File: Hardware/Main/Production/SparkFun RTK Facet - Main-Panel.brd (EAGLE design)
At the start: 138.6 x 187.7 mm, 990 parts, among them J1 QWIIC_RIGHT_ANGLE, J16 QWIIC_RIGHT_ANGLE, J2 U.FL, J21 CORTEX_JTAG_DEBUG_PTH, J24 U.FL, J28 QWIIC_RIGHT_ANGLE, J32 CORTEX_JTAG_DEBUG_PTH, J35 U.FL, J39 QWIIC_RIGHT_ANGLE, J43 CORTEX_JTAG_DEBUG_PTH, J46 U.FL, J50 QWIIC_RIGHT_ANGLE, J54 CORTEX_JTAG_DEBUG_PTH, J57 U.FL, J6 U.FL, J61 QWIIC_RIGHT_ANGLE, J65 CORTEX_JTAG_DEBUG_PTH, J68 U.FL, J72 QWIIC_RIGHT_ANGLE, J76 CORTEX_JTAG_DEBUG_PTH, J79 U.FL, J83 QWIIC_RIGHT_ANGLE, J87 CORTEX_JTAG_DEBUG_PTH, J9 CORTEX_JTAG_DEBUG_PTH, Q1 MBT3904DW1T1, Q10 SIL2308, Q11 MBT3904DW1T1, Q12 SIL2308, Q13 MBT3904DW1T1, Q14 SIL2308, Q15 MBT3904DW1T1, Q16 SIL2308, Q2 MBT3904DW1T1, Q3 SIL2308, Q4 SIL2308, Q5 MBT3904DW1T1, Q6 SIL2308, Q7 MBT3904DW1T1, Q8 SIL2308, Q9 MBT3904DW1T1, U1 74HC4052D, U10 MCP73833, U11 U-BLOX_ZED-F9P, U12 AP2112K-3.3, U13 CH340C, U14 MAX17048, U15 MCP73833, U16 74HC4052D, U17 STLQ015, U18 AP2112K-3.3, U19 USB251XB, U2 3.3V, U20 ESP-WROOM-3232D, U21 3.3V, U22 U-BLOX_ZED-F9P, U23 CH340C, U24 MAX17048, U25 MCP73833, U26 74HC4052D, U27 STLQ015, U28 AP2112K-3.3, U29 USB251XB, U3 U-BLOX_ZED-F9P, U30 ESP-WROOM-3232D, U31 3.3V, U32 U-BLOX_ZED-F9P, U33 CH340C, U34 MAX17048, U35 MCP73833, U36 74HC4052D, U37 STLQ015, U38 AP2112K-3.3, U39 USB251XB, U4 STLQ015, U40 ESP-WROOM-3232D, U41 3.3V, U42 U-BLOX_ZED-F9P, U43 CH340C, U44 MAX17048, U45 MCP73833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

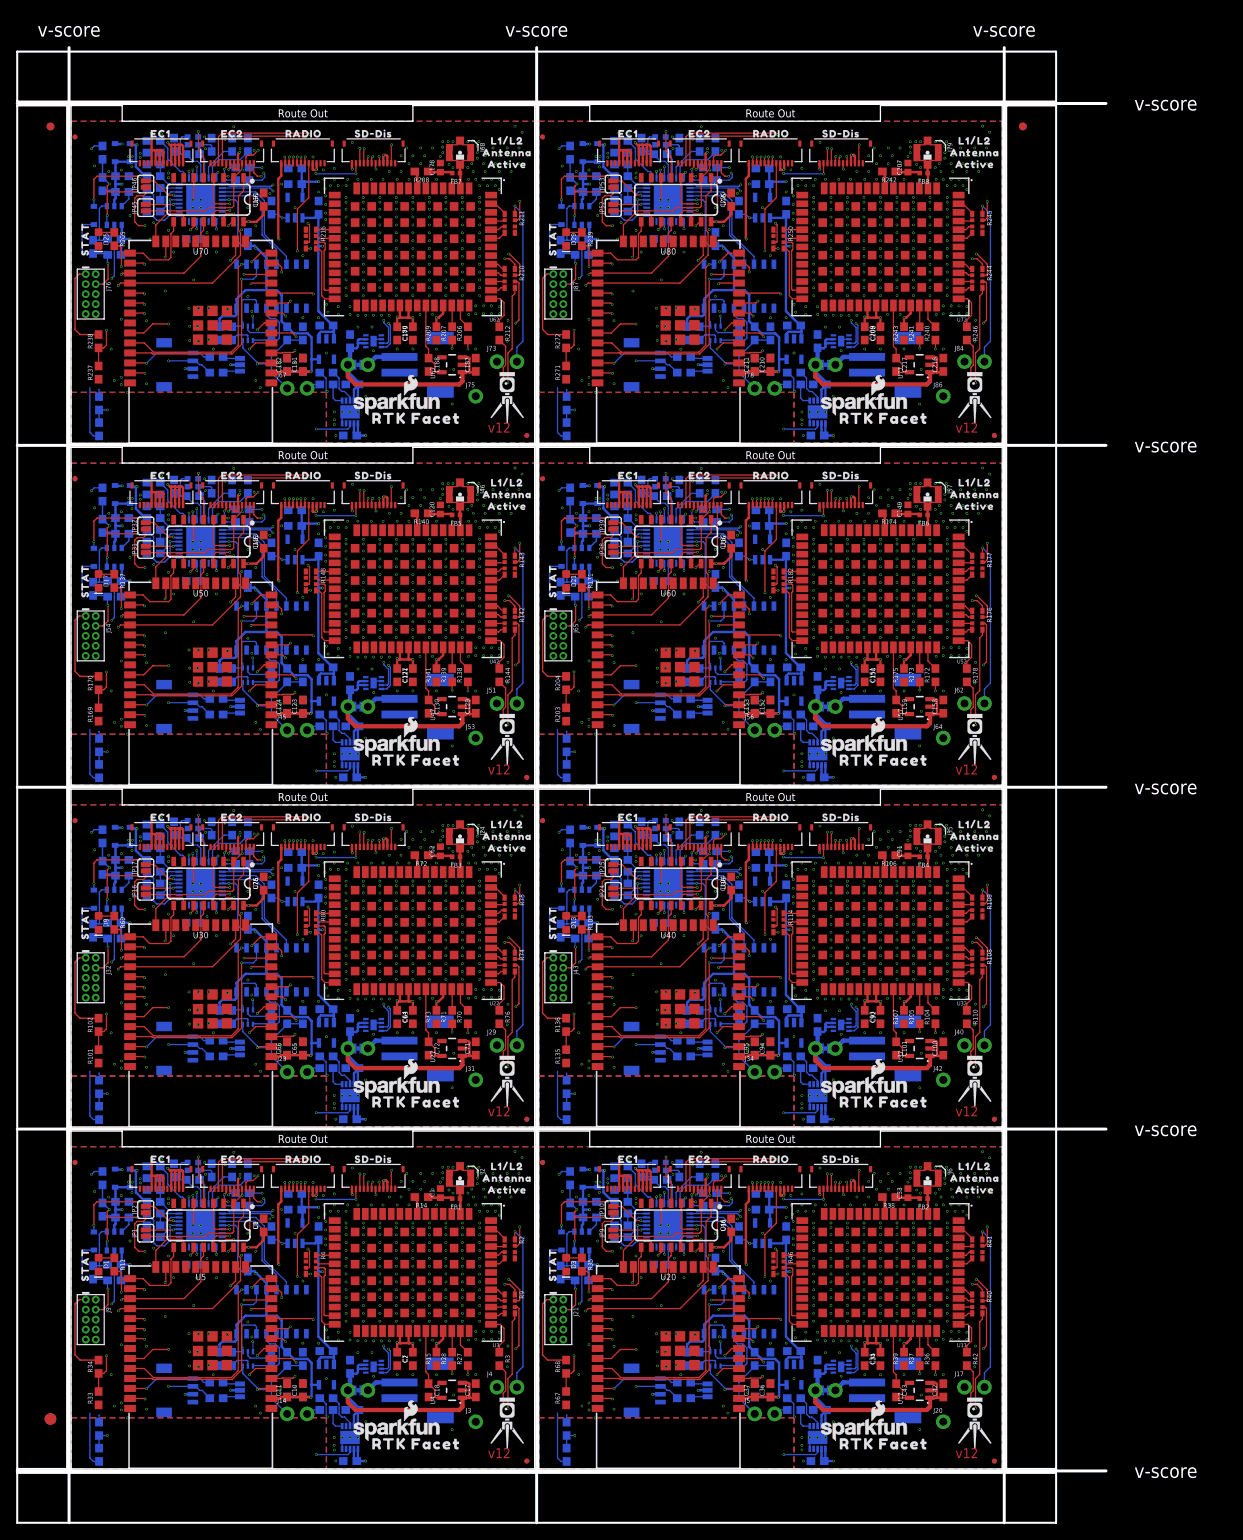
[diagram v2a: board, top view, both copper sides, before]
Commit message: Facet v13: change charger IC FP, discrete 33s, change cream on ESP32.
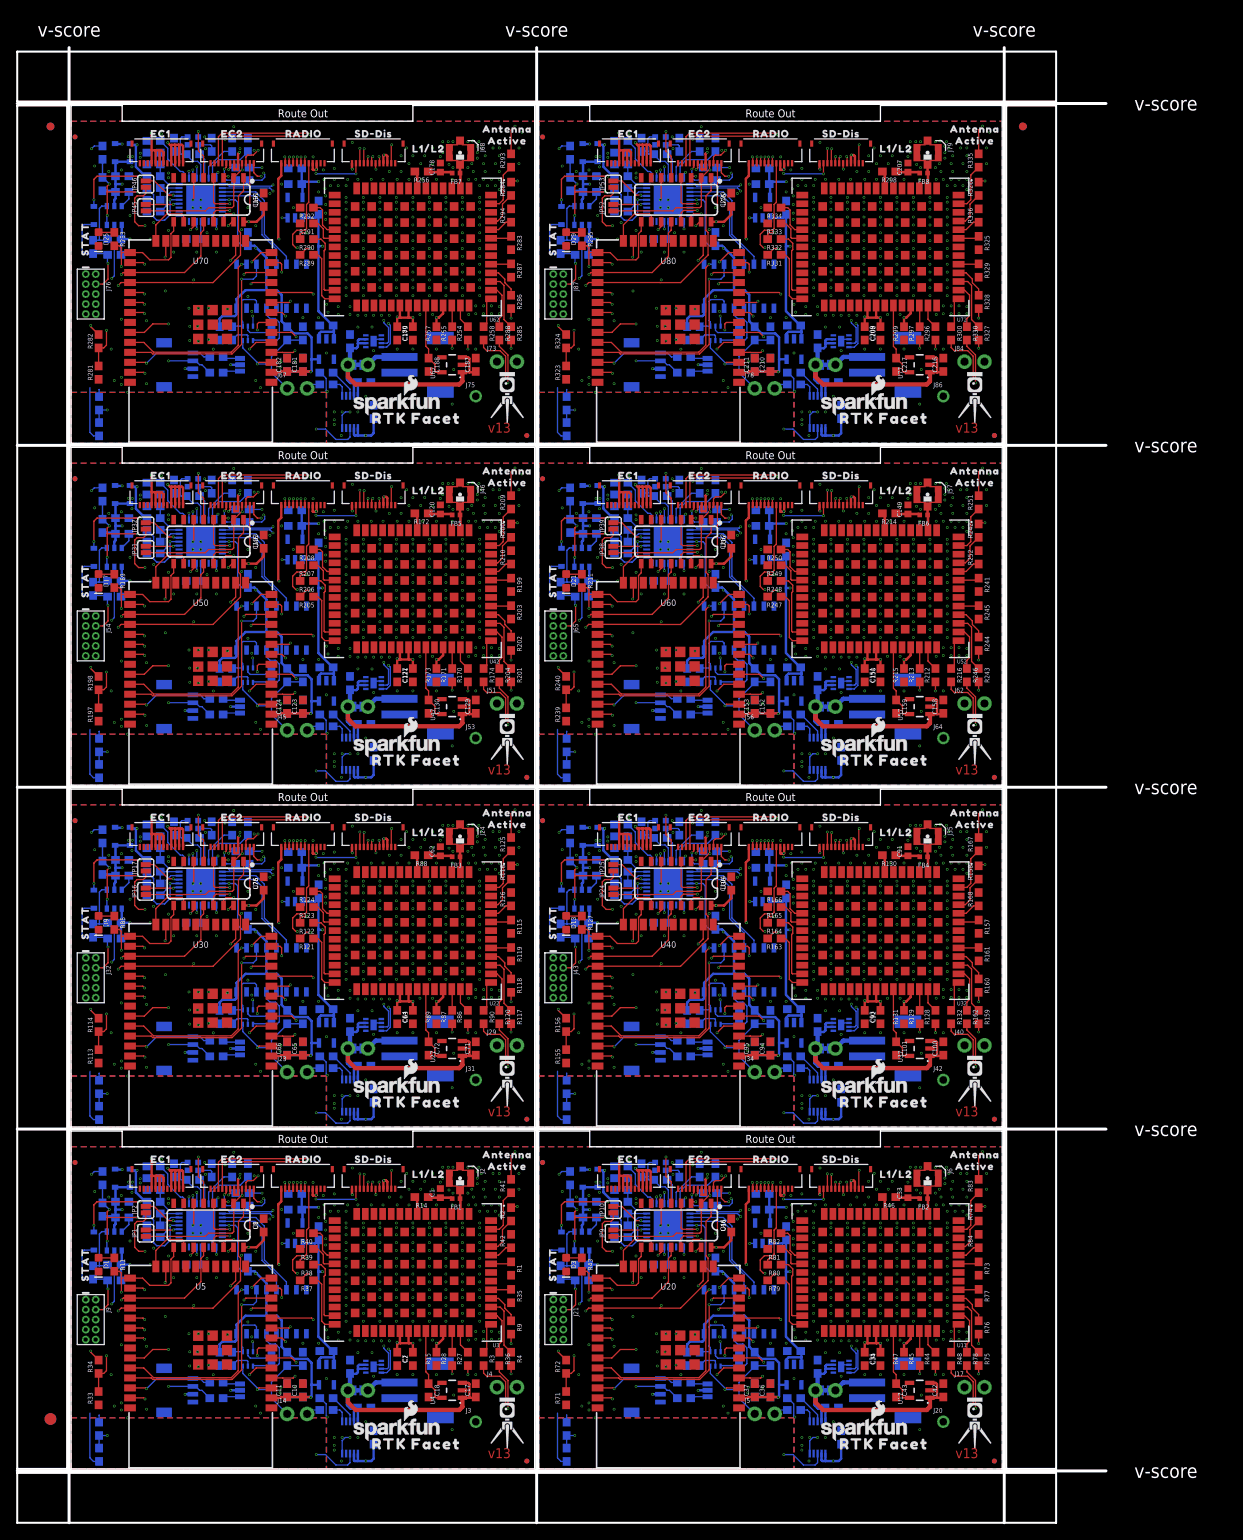
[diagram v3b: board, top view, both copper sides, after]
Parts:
- added R273, R315: 1M, SparkFun-Resistors:0603
- added R274, R275, R276, R277, R278, R299, R312, R316, R317, R318, R319, R320: 100k, SparkFun-Resistors:0603
- added R279, R280, R321, R322: 22Ω, SparkFun-Resistors:0603
- added R281, R282, R301, R302, R303, R307, R310, R313, R323, R324: 10k, SparkFun-Resistors:0603
- added R283, R284, R285, R286, R287, R288, R289, R290, R291, R292, R293, R294, R300, R325, R326, R327, R328, R329, R330, R331, R332, R333, R334, R335, R336: 33, SparkFun-Resistors:0603
- added R295, R304: 1k, SparkFun-Resistors:0603
- added R296, R297: 27, SparkFun-Resistors:0603
- added R298: 10, SparkFun-Resistors:0603
- added R305: 150k, SparkFun-Resistors:0603
- added R306: 0, SparkFun-Resistors:0603
- added R308, R309: 2.2k, SparkFun-Resistors:0603
- added R311: 300k, SparkFun-Resistors:0603
- added R314: 12k, SparkFun-Resistors:0603
- JP1, JP10, JP16, JP17, JP2, JP24, JP25, JP31, JP32, JP38, JP39, JP45, JP46, JP52, JP53, JP9: value (none) -> JUMPER-SMT_2_NO_SILK
- MEAS1, MEAS2, MEAS3, MEAS4, MEAS5, MEAS6, MEAS7, MEAS8: value (none) -> JUMPER-COMBO_2_NC_TRACE
- R1, R123, R125, R132, R157, R159, R162, R163, R164, R165, R166, R199, R200, R209, R243, R39, R73: value 100k -> 33
- R100, R133, R134: value 22 -> 10k
- R101: value 10k -> 300k
- R102, R152, R186, R192, R215, R257, R67, R68: value 10k -> 100k
- R103, R217, R239: value 1k -> 10k
- R104: value 27 -> 12k
- R105: value 27 -> 1M
- R106: value 10 -> 100k
- R108, R109, R148: value 33 -> 100k; device SparkFun-Resistors:1206_RA -> SparkFun-Resistors:0603
- R110, R144: value 33 -> 100k
- R111, R112, R237, R238: value 10k -> 22Ω
- R114, R142, R176, R177: value 33 -> 10k; device SparkFun-Resistors:1206_RA -> SparkFun-Resistors:0603
- R115, R205, R251, R35, R81: value 1k -> 33
- R116, R252, R48, R82: value 150k -> 33
- R117, R83: value 0 -> 33
- R118, R121, R124, R158, R203, R204, R247, R248, R249, R77, R78, R79, R84, R90: value 10k -> 33
- R119, R120: value 2.2k -> 33
- R122, R258: value 300k -> 33
- R126, R160: value 12k -> 33
- R127: value 1M -> 1k
- R128, R129: value 100k -> 27
- R130: value 100k -> 10
- R136, R169, R220, R43: value 10k -> 1k
- R137: value 1k -> 150k
- R138: value 27 -> 0
- R139, R240, R71: value 27 -> 10k
- R140: value 10 -> 2.2k
- R141, R225, R266, R267, R57, R98: value 100k -> 2.2k
- R143: value 33 -> 300k; device SparkFun-Resistors:1206_RA -> SparkFun-Resistors:0603
- R146, R272: value 10k -> 12k
- R147, R189: value 10k -> 1M
- R149, R47: value 1k -> 100k
- R150: value 150k -> 100k
- R151: value 0 -> 100k
- R153, R154: value 2.2k -> 22Ω
- R156: value 300k -> 10k
- R161: value 1M -> 33
- R167, R168, R201, R202: value 22 -> 33
- R170, R213, R254, R44, R45, R87: value 10k -> 27
- R171: value 1k -> 27
- R172: value 27 -> 10
- R173: value 27 -> 100k
- R174, R208, R242, R38: value 10 -> 33
- R175, R197, R198, R259, R261, R265, R268, R55, R61, R91, R97: value 100k -> 10k
- R178: value 33 -> 1k
- R179, R53: value 10k -> 150k
- R180: value 10k -> 0
- R182: value 33 -> 2.2k; device SparkFun-Resistors:1206_RA -> SparkFun-Resistors:0603
- R183: value 1k -> 2.2k
- R184, R218: value 150k -> 10k
- R185: value 0 -> 300k
- R187, R51: value 2.2k -> 10k
- R188: value 2.2k -> 12k
- R190: value 300k -> 100k
- R194, R228: value 12k -> 100k
- R195: value 1M -> 22Ω
- R196: value 100k -> 22Ω
- R2, R210, R216, R244, R245, R250, R4, R40, R41, R74, R75, R80, R9: device SparkFun-Resistors:1206_RA -> SparkFun-Resistors:0603
- R206, R207, R241, R36, R37: value 27 -> 33
- R211: value 33 -> 1k; device SparkFun-Resistors:1206_RA -> SparkFun-Resistors:0603
- R212: value 33 -> 27
- R214: value 10k -> 10
- R219, R49: value 0 -> 10k
- R221: value 2.2k -> 150k
- R222: value 2.2k -> 0
- R224: value 300k -> 2.2k
- R227: value 100k -> 300k
- R229, R93: value 1M -> 10k
- R230, R62: value 100k -> 12k
- R231, R63: value 100k -> 1M
- R235, R236, R270, R65, R66: value 22 -> 100k
- R25, R32: value 22 -> 22Ω
- R253: value 0 -> 1k
- R255, R86: value 2.2k -> 27
- R256: value 2.2k -> 10
- R262: value 12k -> 1k
- R263: value 1M -> 150k
- R264, R96: value 100k -> 0
- R269: value 22 -> 300k
- R46: value 33 -> 10; device SparkFun-Resistors:1206_RA -> SparkFun-Resistors:0603
- R52, R85: value 2.2k -> 1k
- R54: value 300k -> 0
- R56: value 10k -> 2.2k
- R58, R92: value 12k -> 10k
- R59: value 1M -> 300k
- R69: value 1k -> 22Ω
- R70: value 27 -> 22Ω
- R72: value 10 -> 10k
- R88: value 300k -> 10
- R94: value 100k -> 1k
- R95: value 100k -> 150k
- R99: value 22 -> 2.2k
- U10, U15, U25, U35, U45, U55, U65, U75: value MCP73833 -> MCP73833MSOP; device SparkFun-IC-Power:DFN-10 -> SparkFun-IC-Power:MSOP10
- U12, U18, U28, U38, U48, U58, U68, U78: value AP2112K-3.3 -> AP2112K-3.3V
- U2, U21, U31, U41, U51, U61, U71, U9: value 3.3V -> AP2112K-3.3V
- U20, U30, U40, U5, U50, U60, U70, U80: value ESP-WROOM-3232D -> ESP-WROOM-3232D-DFMP; device SparkFun-RF:ESP-WROOM-32D -> SparkFun-RF:ESP-WROOM-32D-DFM_PASTE
- moved R162 123.8 mm to (114.0, 57.5), flipped to the top, turned to 270 degrees
- moved R157 119.9 mm to (115.5, 69.0), flipped to the top, turned to 270 degrees
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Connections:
- net 3.3V1: now also R47.2; no longer R39.2
- net 3.3V2: now also R89.2; no longer R73.2
- net 3.3V3: now also R131.2; no longer R107.2
- net 3.3V4: now also R173.2; no longer R141.2
- net 3.3V5: now also R215.2; no longer R175.2
- net 3.3V6: now also R257.2; no longer R209.2
- net 3.3V7: now also R299.2; no longer R243.2
- net ANT_VCC1: now also R46.1; no longer R38.1
- net ANT_VCC2: now also R88.1; no longer R72.1
- net ANT_VCC3: now also R130.1; no longer R106.1
- net ANT_VCC4: now also R172.1; no longer R140.1
- net ANT_VCC5: now also R214.1; no longer R174.1
- net ANT_VCC6: now also R256.1; no longer R208.1
- net ANT_VCC7: now also R298.1; no longer R242.1
- net CHG_THERM2: now also R53.2, R54.2, R55.2; no longer R48.2, R49.2, R50.2
- net CHG_THERM3: now also R95.2, R96.2, R97.2; no longer R82.2, R83.2, R84.2
- net CHG_THERM4: now also R137.2, R138.2, R139.2; no longer R116.2, R117.2, R118.2
- net CHG_THERM5: now also R179.2, R180.2, R181.2; no longer R150.2, R151.2, R152.2
- net CHG_THERM6: now also R221.2, R222.2, R223.2; no longer R184.2, R185.2, R186.2
- net CHG_THERM7: now also R263.2, R264.2, R265.2; no longer R218.2, R219.2, R220.2
- net CHG_THERM8: now also R305.2, R306.2, R307.2; no longer R252.2, R253.2, R254.2
- net ESP32_!DTR1: now also R50.1; no longer R44.1
- net ESP32_!DTR2: now also R92.1; no longer R78.1
- net ESP32_!DTR3: now also R134.1; no longer R112.1
- net ESP32_!DTR4: now also R176.1; no longer R146.1
- net ESP32_!DTR5: now also R218.1; no longer R180.1
- net ESP32_!DTR6: now also R260.1; no longer R214.1
- net ESP32_!DTR7: now also R302.1; no longer R248.1
- net ESP32_!RTS1: now also R51.1; no longer R45.1
- net ESP32_!RTS2: now also R93.1; no longer R79.1
- net ESP32_!RTS3: now also R135.1; no longer R113.1
- net ESP32_!RTS4: now also R177.1; no longer R147.1
- net ESP32_!RTS5: now also R219.1; no longer R181.1
- net ESP32_!RTS6: now also R261.1; no longer R215.1
- net ESP32_!RTS7: now also R303.1; no longer R249.1
- net ESP32_EN1: now also R49.1; no longer R43.1
- net ESP32_EN2: now also R91.1; no longer R77.1
- net ESP32_EN3: now also R133.1; no longer R111.1
- net ESP32_EN4: now also R175.1; no longer R145.1
- net ESP32_EN5: now also R217.1; no longer R179.1
- net ESP32_EN6: now also R259.1; no longer R213.1
- net ESP32_EN7: now also R301.1; no longer R247.1
- net ESP_0/BOOT/STAT_LED/MUX_B1: now also R43.2; no longer R35.2
- net ESP_0/BOOT/STAT_LED/MUX_B2: now also R85.2; no longer R69.2
- net ESP_0/BOOT/STAT_LED/MUX_B3: now also R127.2; no longer R103.2
- net ESP_0/BOOT/STAT_LED/MUX_B4: now also R169.2; no longer R137.2
- net ESP_0/BOOT/STAT_LED/MUX_B5: now also R211.2; no longer R171.2
- net ESP_0/BOOT/STAT_LED/MUX_B6: now also R253.2; no longer R205.2
- net ESP_0/BOOT/STAT_LED/MUX_B7: now also R295.2; no longer R239.2
- net ESP_13/POWER_CTRL/MTCK1: now also R58.1, R59.2; no longer R53.1, R54.2
- net ESP_13/POWER_CTRL/MTCK2: now also R100.1, R101.2; no longer R87.1, R88.2
- net ESP_13/POWER_CTRL/MTCK3: now also R142.1, R143.2; no longer R121.1, R122.2
- net ESP_13/POWER_CTRL/MTCK4: now also R184.1, R185.2; no longer R155.1, R156.2
- net ESP_13/POWER_CTRL/MTCK5: now also R226.1, R227.2; no longer R189.1, R190.2
- net ESP_13/POWER_CTRL/MTCK6: now also R268.1, R269.2; no longer R223.1, R224.2
- net ESP_13/POWER_CTRL/MTCK7: now also R310.1, R311.2; no longer R257.1, R258.2
- net ESP_14/PERIPHERAL_POWER/MTMS: no longer R1.2
- net ESP_14/PERIPHERAL_POWER/MTMS1: no longer R57.2
- net ESP_14/PERIPHERAL_POWER/MTMS2: no longer R91.2
- net ESP_14/PERIPHERAL_POWER/MTMS3: no longer R125.2
- net ESP_14/PERIPHERAL_POWER/MTMS4: no longer R159.2
- net ESP_14/PERIPHERAL_POWER/MTMS5: no longer R193.2
- net ESP_14/PERIPHERAL_POWER/MTMS6: no longer R227.2
- net ESP_14/PERIPHERAL_POWER/MTMS7: no longer R261.2
- net ESP_16/ZED-TXO2: now also R48.2; no longer R42.2
- net ESP_16/ZED-TXO3: now also R90.2; no longer R76.2
- net ESP_16/ZED-TXO4: now also R132.2; no longer R110.2
- net ESP_16/ZED-TXO5: now also R174.2; no longer R144.2
- net ESP_16/ZED-TXO6: now also R216.2; no longer R178.2
- net ESP_16/ZED-TXO7: now also R258.2; no longer R212.2
- net ESP_16/ZED-TXO8: now also R300.2; no longer R246.2
- net ESP_17/ZED-RXI1: now also R36.2; no longer R9.P5
- net ESP_17/ZED-RXI2: now also R78.2; no longer R40.P5
- net ESP_17/ZED-RXI3: now also R120.2; no longer R74.P5
- net ESP_17/ZED-RXI4: now also R162.2; no longer R108.P5
- net ESP_17/ZED-RXI5: now also R204.2; no longer R142.P5
- net ESP_17/ZED-RXI6: now also R246.2; no longer R176.P5
- net ESP_17/ZED-RXI7: now also R288.2; no longer R210.P5
- net ESP_17/ZED-RXI8: now also R330.2; no longer R244.P5
- net ESP_21/SDA: now also R4.2; no longer R9.P6
- net ESP_21/SDA1: now also R56.1, R75.2; no longer R40.P6, R51.1
- net ESP_21/SDA2: now also R117.2, R98.1; no longer R74.P6, R85.1
- net ESP_21/SDA3: now also R140.1, R159.2; no longer R108.P6, R119.1
- net ESP_21/SDA4: now also R182.1, R201.2; no longer R142.P6, R153.1
- net ESP_21/SDA5: now also R224.1, R243.2; no longer R176.P6, R187.1
- net ESP_21/SDA6: now also R266.1, R285.2; no longer R210.P6, R221.1
- net ESP_21/SDA7: now also R308.1, R327.2; no longer R244.P6, R255.1
- net ESP_22/SCL: now also R9.2; no longer R9.P7
- net ESP_22/SCL1: now also R57.1, R76.2; no longer R40.P7, R52.1
- net ESP_22/SCL2: now also R118.2, R99.1; no longer R74.P7, R86.1
- net ESP_22/SCL3: now also R141.1, R160.2; no longer R108.P7, R120.1
- net ESP_22/SCL4: now also R183.1, R202.2; no longer R142.P7, R154.1
- net ESP_22/SCL5: now also R225.1, R244.2; no longer R176.P7, R188.1
- net ESP_22/SCL6: now also R267.1, R286.2; no longer R210.P7, R222.1
- net ESP_22/SCL7: now also R309.1, R328.2; no longer R244.P7, R256.1
- net ESP_27/FAST_OFF1: now also R59.1; no longer R54.1
- net ESP_27/FAST_OFF2: now also R101.1; no longer R88.1
- net ESP_27/FAST_OFF3: now also R143.1; no longer R122.1
- net ESP_27/FAST_OFF4: now also R185.1; no longer R156.1
- net ESP_27/FAST_OFF5: now also R227.1; no longer R190.1
- net ESP_27/FAST_OFF6: now also R269.1; no longer R224.1
- net ESP_27/FAST_OFF7: now also R311.1; no longer R258.1
- net ESP_3V1: now also R49.2, R66.2, R72.2; no longer R43.2, R62.2, R68.2
- net ESP_3V2: now also R108.2, R114.2, R91.2; no longer R102.2, R77.2, R96.2
- net ESP_3V4: now also R133.2, R150.2, R156.2; no longer R111.2, R130.2, R136.2
- net ESP_3V5: now also R175.2, R192.2, R198.2; no longer R145.2, R164.2, R170.2
- net ESP_3V6: now also R217.2, R234.2, R240.2; no longer R179.2, R198.2, R204.2
- net ESP_3V7: now also R259.2, R276.2, R282.2; no longer R213.2, R232.2, R238.2
- net ESP_3V8: now also R301.2, R318.2, R324.2; no longer R247.2, R266.2, R272.2
- net ESP_I35/DEVICE_SENSE1: now also R71.2, R72.1; no longer R67.2, R68.1
- net ESP_I35/DEVICE_SENSE2: now also R113.2, R114.1; no longer R101.2, R102.1
- net ESP_I35/DEVICE_SENSE3: now also R155.2, R156.1; no longer R135.2, R136.1
- net ESP_I35/DEVICE_SENSE4: now also R197.2, R198.1; no longer R169.2, R170.1
- net ESP_I35/DEVICE_SENSE5: now also R239.2, R240.1; no longer R203.2, R204.1
- net ESP_I35/DEVICE_SENSE6: now also R281.2, R282.1; no longer R237.2, R238.1
- net ESP_I35/DEVICE_SENSE7: now also R323.2, R324.1; no longer R271.2, R272.1
- net FENCE_LV: now also R40.1; no longer R4.P8
- net FENCE_LV1: now also R82.1; no longer R46.P8
- net FENCE_LV2: now also R124.1; no longer R80.P8
- net FENCE_LV3: now also R166.1; no longer R114.P8
- net FENCE_LV4: now also R208.1; no longer R148.P8
- net FENCE_LV5: now also R250.1; no longer R182.P8
- net FENCE_LV6: now also R292.1; no longer R216.P8
- net FENCE_LV7: now also R334.1; no longer R250.P8
- net GND: no longer R1.1, U10.11
- net GND1: now also R52.1, R53.1, R55.1, R62.2, R64.1, R65.1, R71.1; no longer R39.1, R48.1, R50.1, R57.1, R58.2, R60.1, R61.1, R63.1, U15.11
- net GND2: now also R104.2, R106.1, R107.1, R109.1, R113.1, R89.1; no longer R101.1, R73.1, R81.1, R82.1, R84.1, R91.1, R92.2, U25.11
- net GND3: now also R136.1, R137.1, R139.1, R146.2, R148.1, R149.1, R151.1, R155.1; no longer R107.1, R115.1, R116.1, R118.1, R125.1, R126.2, R128.1, R129.1, R135.1, U35.11
- net GND4: now also R173.1, R178.1, R179.1, R181.1, R188.2, R190.1, R191.1, R193.1, R197.1; no longer R141.1, R149.1, R150.1, R152.1, R159.1, R160.2, R162.1, R163.1, R165.1, R169.1, U45.11
- net GND5: now also R215.1, R220.1, R221.1, R223.1, R230.2, R232.1, R233.1, R235.1, R239.1; no longer R175.1, R183.1, R184.1, R186.1, R193.1, R194.2, R196.1, R197.1, R199.1, R203.1, U55.11
- net GND6: now also R257.1, R262.1, R263.1, R265.1, R272.2, R274.1, R275.1, R277.1, R281.1; no longer R209.1, R217.1, R218.1, R220.1, R227.1, R228.2, R230.1, R231.1, R233.1, R237.1, U65.11
- net GND7: now also R299.1, R304.1, R305.1, R307.1, R314.2, R316.1, R317.1, R319.1, R323.1; no longer R243.1, R251.1, R252.1, R254.1, R261.1, R262.2, R264.1, R265.1, R267.1, R271.1, U75.11
- net N$101: now also R169.1; no longer R137.1
- net N$102: now also R170.2; no longer R138.2
- net N$103: now also R171.2; no longer R139.2
- net N$104: now also R172.2; no longer R140.2
- net N$105: now also R199.1; no longer R143.P4
- net N$106: now also R210.1; no longer R143.P3
- net N$107: now also R203.1; no longer R142.P1
- net N$108: now also R176.2; no longer R146.2
- net N$109: now also R177.2; no longer R147.2
- net N$110: now also R180.1; no longer R151.1
- net N$111: now also R182.2; no longer R153.2
- net N$112: now also R183.2; no longer R154.2
- net N$113: now also R200.1; no longer R143.P2
- net N$114: now also R186.1; no longer R157.1
- net N$115: now also R189.2; no longer R161.2
- net N$116: now also R189.1; no longer R161.1
- net N$117: now also R188.1; no longer R160.1
- net N$118: now also R190.2; no longer R162.2
- net N$119: now also R191.2; no longer R163.2
- net N$122: now also R195.2; no longer R167.2
- net N$123: now also R196.2; no longer R168.2
- net N$126: now also R211.1; no longer R171.1
- net N$127: now also R212.2; no longer R172.2
- net N$128: now also R213.2; no longer R173.2
- net N$129: now also R214.2; no longer R174.2
- net N$130: now also R241.1; no longer R177.P4
- net N$131: now also R252.1; no longer R177.P3
- net N$132: now also R245.1; no longer R176.P1
- net N$133: now also R218.2; no longer R180.2
- net N$134: now also R219.2; no longer R181.2
- net N$135: now also R222.1; no longer R185.1
- net N$136: now also R224.2; no longer R187.2
- net N$137: now also R225.2; no longer R188.2
- net N$138: now also R242.1; no longer R177.P2
- net N$139: now also R228.1; no longer R191.1
- net N$140: now also R231.2; no longer R195.2
- net N$141: now also R231.1; no longer R195.1
- net N$142: now also R230.1; no longer R194.1
- net N$143: now also R232.2; no longer R196.2
- net N$144: now also R233.2; no longer R197.2
- net N$147: now also R237.2; no longer R201.2
- net N$148: now also R238.2; no longer R202.2
- net N$151: now also R253.1; no longer R205.1
- net N$152: now also R254.2; no longer R206.2
- net N$153: now also R255.2; no longer R207.2
- net N$154: now also R256.2; no longer R208.2
- net N$155: now also R283.1; no longer R211.P4
- net N$156: now also R294.1; no longer R211.P3
- net N$157: now also R287.1; no longer R210.P1
- net N$158: now also R260.2; no longer R214.2
- net N$159: now also R261.2; no longer R215.2
- net N$16: now also R1.1; no longer R2.P4
- net N$160: now also R264.1; no longer R219.1
- net N$161: now also R266.2; no longer R221.2
- net N$162: now also R267.2; no longer R222.2
- net N$163: now also R284.1; no longer R211.P2
- net N$164: now also R270.1; no longer R225.1
- net N$165: now also R273.2; no longer R229.2
- net N$166: now also R273.1; no longer R229.1
- net N$167: now also R272.1; no longer R228.1
- net N$168: now also R274.2; no longer R230.2
- net N$169: now also R275.2; no longer R231.2
- net N$172: now also R279.2; no longer R235.2
- net N$173: now also R280.2; no longer R236.2
- net N$176: now also R295.1; no longer R239.1
- net N$177: now also R296.2; no longer R240.2
- net N$178: now also R297.2; no longer R241.2
- net N$179: now also R298.2; no longer R242.2
- net N$18: now also R42.1; no longer R2.P3
- net N$180: now also R325.1; no longer R245.P4
- net N$181: now also R336.1; no longer R245.P3
- net N$182: now also R329.1; no longer R244.P1
- net N$183: now also R302.2; no longer R248.2
- net N$184: now also R303.2; no longer R249.2
- net N$185: now also R306.1; no longer R253.1
- net N$186: now also R308.2; no longer R255.2
- net N$187: now also R309.2; no longer R256.2
- net N$188: now also R326.1; no longer R245.P2
- net N$189: now also R312.1; no longer R259.1
- net N$190: now also R315.2; no longer R263.2
- net N$191: now also R315.1; no longer R263.1
- net N$192: now also R314.1; no longer R262.1
- net N$193: now also R316.2; no longer R264.2
- net N$194: now also R317.2; no longer R265.2
- net N$197: now also R321.2; no longer R269.2
- net N$198: now also R322.2; no longer R270.2
- net N$22: now also R35.1; no longer R9.P1
- net N$26: now also R43.1; no longer R35.1
- net N$27: now also R44.2; no longer R36.2
- net N$28: now also R45.2; no longer R37.2
- net N$29: now also R46.2; no longer R38.2
- net N$30: now also R73.1; no longer R41.P4
- net N$31: now also R84.1; no longer R41.P3
- net N$32: now also R77.1; no longer R40.P1
- net N$33: now also R50.2; no longer R44.2
- net N$34: now also R51.2; no longer R45.2
- net N$35: now also R54.1; no longer R49.1
- net N$36: now also R56.2; no longer R51.2
- net N$37: now also R57.2; no longer R52.2
- net N$38: now also R74.1; no longer R41.P2
- net N$39: now also R60.1; no longer R55.1
- net N$40: now also R63.2; no longer R59.2
- net N$41: now also R63.1; no longer R59.1
- net N$42: now also R62.1; no longer R58.1
- net N$43: now also R64.2; no longer R60.2
- net N$44: now also R65.2; no longer R61.2
- net N$47: now also R69.2; no longer R65.2
- net N$48: now also R70.2; no longer R66.2
- net N$5: now also R2.1; no longer R2.P2
- net N$51: now also R85.1; no longer R69.1
- net N$52: now also R86.2; no longer R70.2
- net N$53: now also R87.2; no longer R71.2
- net N$54: now also R88.2; no longer R72.2
- net N$55: now also R115.1; no longer R75.P4
- net N$56: now also R126.1; no longer R75.P3
- net N$57: now also R119.1; no longer R74.P1
- net N$58: now also R92.2; no longer R78.2
- net N$59: now also R93.2; no longer R79.2
- net N$60: now also R96.1; no longer R83.1
- net N$61: now also R98.2; no longer R85.2
- net N$62: now also R99.2; no longer R86.2
- net N$63: now also R116.1; no longer R75.P2
- net N$64: now also R102.1; no longer R89.1
- net N$65: now also R105.2; no longer R93.2
- net N$66: now also R105.1; no longer R93.1
- net N$67: now also R104.1; no longer R92.1
- net N$68: now also R106.2; no longer R94.2
- net N$69: now also R107.2; no longer R95.2
- net N$72: now also R111.2; no longer R99.2
- net N$73: now also R112.2; no longer R100.2
- net N$76: now also R127.1; no longer R103.1
- net N$77: now also R128.2; no longer R104.2
- net N$78: now also R129.2; no longer R105.2
- net N$79: now also R130.2; no longer R106.2
- net N$80: now also R157.1; no longer R109.P4
- net N$81: now also R168.1; no longer R109.P3
- net N$82: now also R161.1; no longer R108.P1
- net N$83: now also R134.2; no longer R112.2
- net N$84: now also R135.2; no longer R113.2
- net N$85: now also R138.1; no longer R117.1
- net N$86: now also R140.2; no longer R119.2
- net N$87: now also R141.2; no longer R120.2
- net N$88: now also R158.1; no longer R109.P2
- net N$89: now also R144.1; no longer R123.1
- net N$90: now also R147.2; no longer R127.2
- net N$91: now also R147.1; no longer R127.1
- net N$92: now also R146.1; no longer R126.1
- net N$93: now also R148.2; no longer R128.2
- net N$94: now also R149.2; no longer R129.2
- net N$97: now also R153.2; no longer R133.2
- net N$98: now also R154.2; no longer R134.2
- net POWER_BTN1: now also R61.1; no longer R56.1
- net POWER_BTN2: now also R103.1; no longer R90.1
- net POWER_BTN3: now also R145.1; no longer R124.1
- net POWER_BTN4: now also R187.1; no longer R158.1
- net POWER_BTN5: now also R229.1; no longer R192.1
- net POWER_BTN6: now also R271.1; no longer R226.1
- net POWER_BTN7: now also R313.1; no longer R260.1
- net PPS: now also R41.1; no longer R2.P1
- net PPS1: now also R83.1; no longer R41.P1
- net PPS2: now also R125.1; no longer R75.P1
- net PPS3: now also R167.1; no longer R109.P1
- net PPS4: now also R209.1; no longer R143.P1
- net PPS5: now also R251.1; no longer R177.P1
- net PPS6: now also R293.1; no longer R211.P1
- net PPS7: now also R335.1; no longer R245.P1
- net PROG2: now also R52.2; no longer R47.2
- net PROG3: now also R94.2; no longer R81.2
- net PROG4: now also R136.2; no longer R115.2
- net PROG5: now also R178.2; no longer R149.2
- net PROG6: now also R220.2; no longer R183.2
- net PROG7: now also R262.2; no longer R217.2
- net PROG8: now also R304.2; no longer R251.2
- net RTK_LV: now also R39.1; no longer R4.P7
- net RTK_LV1: now also R81.1; no longer R46.P7
- net RTK_LV2: now also R123.1; no longer R80.P7
- net RTK_LV3: now also R165.1; no longer R114.P7
- net RTK_LV4: now also R207.1; no longer R148.P7
- net RTK_LV5: now also R249.1; no longer R182.P7
- net RTK_LV6: now also R291.1; no longer R216.P7
- net RTK_LV7: now also R333.1; no longer R250.P7
- net RX2_LV: now also R38.1; no longer R4.P6
- net RX2_LV1: now also R80.1; no longer R46.P6
- net RX2_LV2: now also R122.1; no longer R80.P6
- net RX2_LV3: now also R164.1; no longer R114.P6
- net RX2_LV4: now also R206.1; no longer R148.P6
- net RX2_LV5: now also R248.1; no longer R182.P6
- net RX2_LV6: now also R290.1; no longer R216.P6
- net RX2_LV7: now also R332.1; no longer R250.P6
- net RXLV: now also R36.1; no longer R9.P4
- net RXLV1: now also R78.1; no longer R40.P4
- net RXLV2: now also R120.1; no longer R74.P4
- net RXLV3: now also R162.1; no longer R108.P4
- net RXLV4: now also R204.1; no longer R142.P4
- net RXLV5: now also R246.1; no longer R176.P4
- net RXLV6: now also R288.1; no longer R210.P4
- net RXLV7: now also R330.1; no longer R244.P4
- net SCL_LV: now also R9.1; no longer R9.P2
- net SCL_LV1: now also R76.1; no longer R40.P2
- net SCL_LV2: now also R118.1; no longer R74.P2
- net SCL_LV3: now also R160.1; no longer R108.P2
- net SCL_LV4: now also R202.1; no longer R142.P2
- net SCL_LV5: now also R244.1; no longer R176.P2
- net SCL_LV6: now also R286.1; no longer R210.P2
- net SCL_LV7: now also R328.1; no longer R244.P2
- net SDA_LV: now also R4.1; no longer R9.P3
- net SDA_LV1: now also R75.1; no longer R40.P3
- net SDA_LV2: now also R117.1; no longer R74.P3
- net SDA_LV3: now also R159.1; no longer R108.P3
- net SDA_LV4: now also R201.1; no longer R142.P3
- net SDA_LV5: now also R243.1; no longer R176.P3
- net SDA_LV6: now also R285.1; no longer R210.P3
- net SDA_LV7: now also R327.1; no longer R244.P3
- net TX2_LV: now also R37.1; no longer R4.P5
- net TX2_LV1: now also R79.1; no longer R46.P5
- net TX2_LV2: now also R121.1; no longer R80.P5
- net TX2_LV3: now also R163.1; no longer R114.P5
- net TX2_LV4: now also R205.1; no longer R148.P5
- net TX2_LV5: now also R247.1; no longer R182.P5
- net TX2_LV6: now also R289.1; no longer R216.P5
- net TX2_LV7: now also R331.1; no longer R250.P5
- net TXLV1: now also R48.1; no longer R42.1
- net TXLV2: now also R90.1; no longer R76.1
- net TXLV3: now also R132.1; no longer R110.1
- net TXLV4: now also R174.1; no longer R144.1
- net TXLV5: now also R216.1; no longer R178.1
- net TXLV6: now also R258.1; no longer R212.1
- net TXLV7: now also R300.1; no longer R246.1
- net USB_!RESET1: now also R66.1; no longer R62.1
- net USB_!RESET2: now also R108.1; no longer R96.1
- net USB_!RESET3: now also R150.1; no longer R130.1
- net USB_!RESET4: now also R192.1; no longer R164.1
- net USB_!RESET5: now also R234.1; no longer R198.1
- net USB_!RESET6: now also R276.1; no longer R232.1
- net USB_!RESET7: now also R318.1; no longer R266.1
- net USB_DM1: now also R69.1; no longer R65.1
- net USB_DM2: now also R111.1; no longer R99.1
- net USB_DM3: now also R153.1; no longer R133.1
- net USB_DM4: now also R195.1; no longer R167.1
- net USB_DM5: now also R237.1; no longer R201.1
- net USB_DM6: now also R279.1; no longer R235.1
- net USB_DM7: now also R321.1; no longer R269.1
- net USB_DP1: now also R70.1; no longer R66.1
- net USB_DP2: now also R112.1; no longer R100.1
- net USB_DP3: now also R154.1; no longer R134.1
- net USB_DP4: now also R196.1; no longer R168.1
- net USB_DP5: now also R238.1; no longer R202.1
- net USB_DP6: now also R280.1; no longer R236.1
- net USB_DP7: now also R322.1; no longer R270.1
- net VBUS_DET1: now also R67.2, R68.1; no longer R63.2, R64.1
- net VBUS_DET2: now also R109.2, R110.1; no longer R97.2, R98.1
- net VBUS_DET3: now also R151.2, R152.1; no longer R131.2, R132.1
- net VBUS_DET4: now also R193.2, R194.1; no longer R165.2, R166.1
- net VBUS_DET5: now also R235.2, R236.1; no longer R199.2, R200.1
- net VBUS_DET6: now also R277.2, R278.1; no longer R233.2, R234.1
- net VBUS_DET7: now also R319.2, R320.1; no longer R267.2, R268.1
- net VOUT1: now also R58.2; no longer R53.2
- net VOUT2: now also R100.2; no longer R87.2
- net VOUT3: now also R142.2; no longer R121.2
- net VOUT4: now also R184.2; no longer R155.2
- net VOUT5: now also R226.2; no longer R189.2
- net VOUT6: now also R268.2; no longer R223.2
- net VOUT7: now also R310.2; no longer R257.2
- net V_RAW1: now also R60.2, R61.2; no longer R55.2, R56.2
- net V_RAW2: now also R102.2, R103.2; no longer R89.2, R90.2
- net V_RAW3: now also R144.2, R145.2; no longer R123.2, R124.2
- net V_RAW4: now also R186.2, R187.2; no longer R157.2, R158.2
- net V_RAW5: now also R228.2, R229.2; no longer R191.2, R192.2
- net V_RAW6: now also R270.2, R271.2; no longer R225.2, R226.2
- net V_RAW7: now also R312.2, R313.2; no longer R259.2, R260.2
- net V_USB1: now also R68.2; no longer R64.2
- net V_USB2: now also R110.2; no longer R98.2
- net V_USB3: now also R152.2; no longer R132.2
- net V_USB4: now also R194.2; no longer R166.2
- net V_USB5: now also R236.2; no longer R200.2
- net V_USB6: now also R278.2; no longer R234.2
- net V_USB7: now also R320.2; no longer R268.2
- net ZED-RXI1: now also R80.2; no longer R46.P3
- net ZED-RXI2: now also R38.2; no longer R4.P3
- net ZED-RXI3: now also R122.2; no longer R80.P3
- net ZED-RXI4: now also R164.2; no longer R114.P3
- net ZED-RXI5: now also R206.2; no longer R148.P3
- net ZED-RXI6: now also R248.2; no longer R182.P3
- net ZED-RXI7: now also R290.2; no longer R216.P3
- net ZED-RXI8: now also R332.2; no longer R250.P3
- net ZED-TXO1: now also R79.2; no longer R46.P4
- net ZED-TXO2: now also R37.2; no longer R4.P4
- net ZED-TXO3: now also R121.2; no longer R80.P4
- net ZED-TXO4: now also R163.2; no longer R114.P4
- net ZED-TXO5: now also R205.2; no longer R148.P4
- net ZED-TXO6: now also R247.2; no longer R182.P4
- net ZED-TXO7: now also R289.2; no longer R216.P4
- net ZED-TXO8: now also R331.2; no longer R250.P4
- net ZED_!RESET!: now also R1.2; no longer R2.P5
- net ZED_!RESET!1: now also R73.2; no longer R41.P5
- net ZED_!RESET!2: now also R115.2; no longer R75.P5
- net ZED_!RESET!3: now also R157.2; no longer R109.P5
- net ZED_!RESET!4: now also R199.2; no longer R143.P5
- net ZED_!RESET!5: now also R241.2; no longer R177.P5
- net ZED_!RESET!6: now also R283.2; no longer R211.P5
- net ZED_!RESET!7: now also R325.2; no longer R245.P5
- net ZED_!SAFE!: now also R42.2; no longer R2.P6
- net ZED_!SAFE!1: now also R84.2; no longer R41.P6
- net ZED_!SAFE!2: now also R126.2; no longer R75.P6
- net ZED_!SAFE!3: now also R168.2; no longer R109.P6
- net ZED_!SAFE!4: now also R210.2; no longer R143.P6
- net ZED_!SAFE!5: now also R252.2; no longer R177.P6
- net ZED_!SAFE!6: now also R294.2; no longer R211.P6
- net ZED_!SAFE!7: now also R336.2; no longer R245.P6
- net ZED_DM1: now also R45.1; no longer R37.1
- net ZED_DM2: now also R87.1; no longer R71.1
- net ZED_DM3: now also R129.1; no longer R105.1
- net ZED_DM4: now also R171.1; no longer R139.1
- net ZED_DM5: now also R213.1; no longer R173.1
- net ZED_DM6: now also R255.1; no longer R207.1
- net ZED_DM7: now also R297.1; no longer R241.1
- net ZED_DP1: now also R44.1; no longer R36.1
- net ZED_DP2: now also R86.1; no longer R70.1
- net ZED_DP3: now also R128.1; no longer R104.1
- net ZED_DP4: now also R170.1; no longer R138.1
- net ZED_DP5: now also R212.1; no longer R172.1
- net ZED_DP6: now also R254.1; no longer R206.1
- net ZED_DP7: now also R296.1; no longer R240.1
- net ZED_EXTINT: now also R2.2; no longer R2.P7
- net ZED_EXTINT1: now also R74.2; no longer R41.P7
- net ZED_EXTINT2: now also R116.2; no longer R75.P7
- net ZED_EXTINT3: now also R158.2; no longer R109.P7
- net ZED_EXTINT4: now also R200.2; no longer R143.P7
- net ZED_EXTINT5: now also R242.2; no longer R177.P7
- net ZED_EXTINT6: now also R284.2; no longer R211.P7
- net ZED_EXTINT7: now also R326.2; no longer R245.P7
- net ZED_FENCE_STAT: now also R40.2; no longer R4.P1
- net ZED_FENCE_STAT1: now also R82.2; no longer R46.P1
- net ZED_FENCE_STAT2: now also R124.2; no longer R80.P1
- net ZED_FENCE_STAT3: now also R166.2; no longer R114.P1
- net ZED_FENCE_STAT4: now also R208.2; no longer R148.P1
- net ZED_FENCE_STAT5: now also R250.2; no longer R182.P1
- net ZED_FENCE_STAT6: now also R292.2; no longer R216.P1
- net ZED_FENCE_STAT7: now also R334.2; no longer R250.P1
- net ZED_PPS_STAT: now also R41.2; no longer R2.P8
- net ZED_PPS_STAT1: now also R83.2; no longer R41.P8
- net ZED_PPS_STAT2: now also R125.2; no longer R75.P8
- net ZED_PPS_STAT3: now also R167.2; no longer R109.P8
- net ZED_PPS_STAT4: now also R209.2; no longer R143.P8
- net ZED_PPS_STAT5: now also R251.2; no longer R177.P8
- net ZED_PPS_STAT6: now also R293.2; no longer R211.P8
- net ZED_PPS_STAT7: now also R335.2; no longer R245.P8
- net ZED_RTK_STAT: now also R39.2; no longer R4.P2
- net ZED_RTK_STAT1: now also R81.2; no longer R46.P2
- net ZED_RTK_STAT2: now also R123.2; no longer R80.P2
- net ZED_RTK_STAT3: now also R165.2; no longer R114.P2
- net ZED_RTK_STAT4: now also R207.2; no longer R148.P2
- net ZED_RTK_STAT5: now also R249.2; no longer R182.P2
- net ZED_RTK_STAT6: now also R291.2; no longer R216.P2
- net ZED_RTK_STAT7: now also R333.2; no longer R250.P2
- net ZED_TX_READY: now also R35.2; no longer R9.P8
- net ZED_TX_READY1: now also R77.2; no longer R40.P8
- net ZED_TX_READY2: now also R119.2; no longer R74.P8
- net ZED_TX_READY3: now also R161.2; no longer R108.P8
- net ZED_TX_READY4: now also R203.2; no longer R142.P8
- net ZED_TX_READY5: now also R245.2; no longer R176.P8
- net ZED_TX_READY6: now also R287.2; no longer R210.P8
- net ZED_TX_READY7: now also R329.2; no longer R244.P8
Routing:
- net ZED_TX_READY4: track 12.8 -> 0.00 mm, vias 2 -> 0
- net ZED_TX_READY5: track 12.8 -> 0.00 mm, vias 2 -> 0
- net ZED_TX_READY: track 12.8 -> 0.00 mm, vias 2 -> 0
- net ZED_TX_READY1: track 12.8 -> 0.00 mm, vias 2 -> 0
- net ZED_TX_READY2: track 12.8 -> 0.00 mm, vias 2 -> 0
- net ZED_TX_READY3: track 12.8 -> 0.00 mm, vias 2 -> 0
- net ZED_TX_READY6: track 12.8 -> 0.00 mm, vias 2 -> 0
- net ZED_TX_READY7: track 12.8 -> 0.00 mm, vias 2 -> 0
- net ESP_22/SCL7: track 141.2 -> 130.6 mm, vias 10 -> 9
- net ESP_22/SCL: track 141.2 -> 130.6 mm, vias 10 -> 9
- net ESP_22/SCL6: track 141.2 -> 130.6 mm, vias 10 -> 9
- net ESP_22/SCL4: track 141.2 -> 130.6 mm, vias 10 -> 9
- net ESP_22/SCL2: track 141.2 -> 130.6 mm, vias 10 -> 9
- net ESP_22/SCL1: track 141.2 -> 130.6 mm, vias 10 -> 9
- net ESP_22/SCL5: track 141.2 -> 130.6 mm, vias 10 -> 9
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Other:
- board text added: "v13"
- board text removed: "v12"
